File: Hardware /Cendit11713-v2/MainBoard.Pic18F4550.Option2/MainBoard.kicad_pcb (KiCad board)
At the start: 2 copper layers, 90 parts, among them CON1 POWER_BUS, CON2 ICSP_CON, CON3 USB_CON, J1 RESET_CON, J2 SATA_PLUG _22P_SMT, J4 SATA_PLUG _22P_SMT, P1 DEBUG_HEADER_21P, P2 DEBUG_HEADER_21P, Q1 2N2222, U1 PIC18F4550-I/P, U2 MPL3115A2, U3 PCF85263A, Y1 Crystal, Y2 32.768KHZ

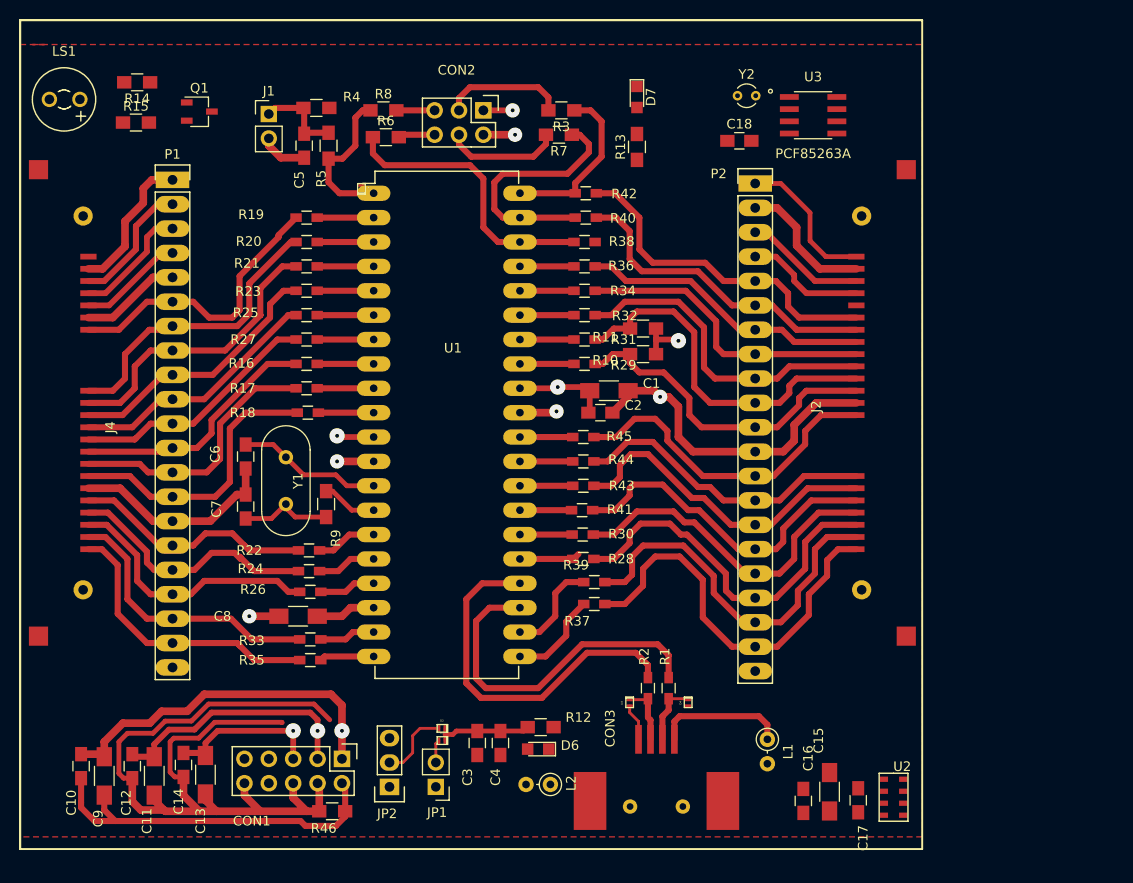
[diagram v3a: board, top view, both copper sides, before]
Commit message: En CenditLab + Cendit11713
   - Diseño de clases UI para Steps (TaskExecutionStep)
   - Layout PCB tarjeta madre opcion 2
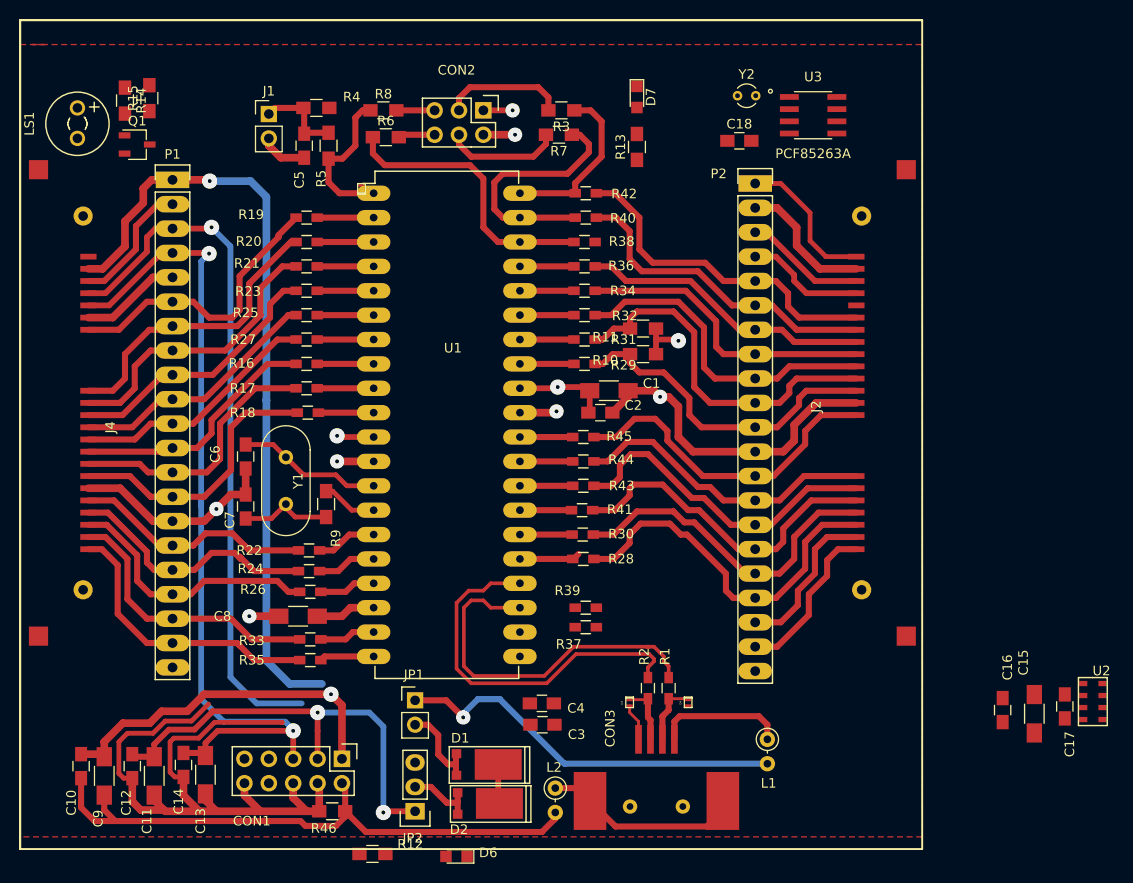
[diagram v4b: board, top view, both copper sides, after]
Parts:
- D1, D2: value SP1003-01ETG -> DST5100S; footprint CenditFootprints2:SP1003-01ETG -> CenditFootprints:DST5100S-TO-277B
- moved C17 23.6 mm to (254.9, 122.3)
- moved U2 23.0 mm to (257.8, 121.8)
- moved C15 22.8 mm to (251.7, 123.1)
- moved C16 22.8 mm to (248.4, 122.7)
- moved R12 21.9 mm to (182.8, 137.7)
- moved D6 14.0 mm to (191.5, 137.9)
- moved JP1 9.27 mm to (187.2, 121.7), turned to 0 degrees
- moved Q1 7.33 mm to (158.2, 63.8)
- moved C3 7.06 mm to (200.5, 124.2), turned to 0 degrees
- moved D2 6.33 mm to (191.1, 130.8), turned to 0 degrees
- moved C4 5.97 mm to (200.4, 122.0), turned to 0 degrees
- moved LS1 5.00 mm to (152.0, 63.1), turned to 90 degrees
- moved JP2 3.68 mm to (187.2, 133.2)
- moved R15 2.90 mm to (159.5, 58.9), turned to 90 degrees
- moved R39 2.81 mm to (205.0, 112.0)
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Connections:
- CON1 pad 7: (no net) -> Net-(CON1-Pad7)
- CON1 pad 8: (no net) -> Net-(CON1-Pad8)
- CON1 pad 9: (no net) -> Net-(CON1-Pad9)
- D5 pad 2: (no net) -> Net-(D5-Pad2)
- J4 pad 1: (no net) -> Net-(J4-Pad1)
- P1 pad 21: (no net) -> Net-(P1-Pad21)
- P1 pad 4: /VCC_3V -> /VDD_3V
- P2 pad 21: (no net) -> Net-(P2-Pad21)
- P2 pad 4: /VCC_3V -> /VDD_3V
- R38 pad 2: (no net) -> /PB5
- U2 pad 5: (no net) -> Net-(U2-Pad5)
- U2 pad 6: (no net) -> Net-(U2-Pad6)
- U3 pad 3: (no net) -> Net-(BT1-Pad1)
- U3 pad 7: (no net) -> Net-(U3-Pad7)
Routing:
- net /VCC_5V: track 52.8 -> 133.7 mm, vias 1 -> 3
- net /VDD_3V: track 16.3 -> 94.6 mm, vias 1 -> 2
- net /VPWR: track 67.4 -> 133.3 mm, vias 1 -> 2
- net /USB_VBUS: track 0.00 -> 41.2 mm, vias 0 -> 1
- net //RST_KEY: track 41.9 -> 17.0 mm
- net GNDPWR: track 52.0 -> 76.0 mm
- net //RST_GPIB: track 39.3 -> 17.9 mm
- net Net-(CON3-Pad5): track 0.00 -> 20.8 mm
- net /VCC_3V: track 23.5 -> 7.37 mm
- net GNDD: track 177.3 -> 164.3 mm, vias 5 -> 6
- net /RD3: track 10.2 -> 0.00 mm
- net /RD2: track 9.78 -> 0.00 mm
- net Net-(D1-Pad2): track 2.41 -> 9.45 mm
- net VDD: track 32.3 -> 26.2 mm
- net /USB_D-: track 37.0 -> 38.5 mm
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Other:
- net class USB_PAIR: trace_width 0.25 -> 0.381; via_dia 0.6 -> 1.5
